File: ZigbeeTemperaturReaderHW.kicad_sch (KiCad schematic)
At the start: 0 parts

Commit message: schema and placed
Draw full schematic (ESP32-C6-Zero, OLED, DS18B20 jack connectors,
LDO regulator, battery holder, pairing button, I2C pull-ups) and wire
all nets with global labels and power symbols. Add footprint library
table entries and component reference documentation.

Co-Authored-By: Claude Sonnet 5 <noreply@anthropic.com>
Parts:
- added BAT2: (no value), Mechanical:BatteryHolder_3xAAA, symbol Mechanical:BatteryHolder_3xAAA
- added C1, C2, C4, C5: CC1206KRX7R9BB104, symbol Passive:Capacitor
- added C6: CC1206KKX7RDBB102, symbol Passive:Capacitor
- added JP1, JP2: (no value), Connectors:JY039-5P, symbol Connector:JY039-5P
- added OLED2: (no value), Modules:OLED-0.96-SSD1306-I2C, symbol Modules:OLED096
- added R1, R2, R3, R4: RC1206JR-7W1RLC19632287, symbol Passive:Resistor
- added S2: TL1105BF160Q, Mechanical:SW_TL1105BF160Q, symbol Mechanical:TL1105BF160Q
- added U1: (no value), Modules:Waveshare-ESP32-C6-Zero, symbol Modules:Waveshare-ESP32-C6-Zero
- added U2: RT9080-33GJ5, Power:TSOT-23-5_RIT-L, symbol Power:RT9080-33GJ5
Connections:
- new net: BAT2.1 (VCC4V5), C2.1, U2.1 (VIN), U2.3 (EN)
- new net GND: BAT2.2 (GND), C1.2, C2.2, C4.2, C5.2, C6.2, JP1.1, JP2.1, OLED2.1 (GND), S2.3, S2.4, U1.2 (GND), U2.2 (GND)
- new net OLED_SCL: OLED2.3 (SCL), R3.2, U1.13 (IO19)
- new net OLED_SDA: OLED2.4 (SDA), R2.2, U1.14 (IO18)
- new net ONE_WIRE: C6.1, JP1.3, JP2.3, R1.2, U1.6 (IO2)
- new net PAIRING: C4.1, R4.2, S2.1, S2.2, U1.8 (IO4)
- new net SENSOR_POWER: C5.1, JP1.5, JP2.5, R1.1, U1.7 (IO3)
- new net VCC3V3: C1.1, OLED2.2 (VCC), R2.1, R3.1, R4.1, U1.3 (V3V), U2.5 (VOUT)
- no-connect marks 0 -> 16

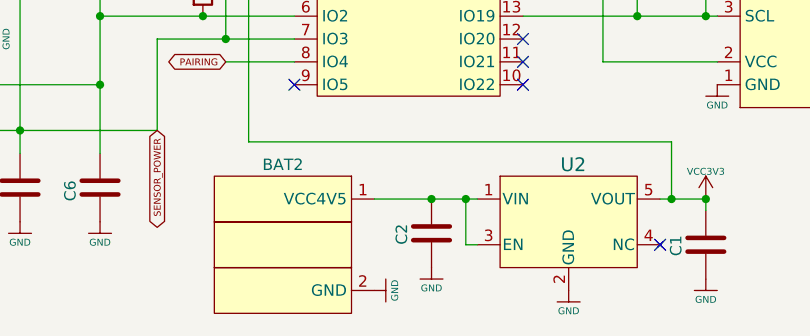
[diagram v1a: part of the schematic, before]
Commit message: Add board dimensions and JLCPCB Gerber/drill export
- Add overall width/height dimension annotations (48.00 x 74.00 mm)
  on the Dwgs.User layer
- Include schematic edits made in the KiCad session
- Add Gerber and Excellon drill files for JLCPCB ordering, plus a
  ready-to-upload ZIP archive

Co-Authored-By: Claude Sonnet 5 <noreply@anthropic.com>
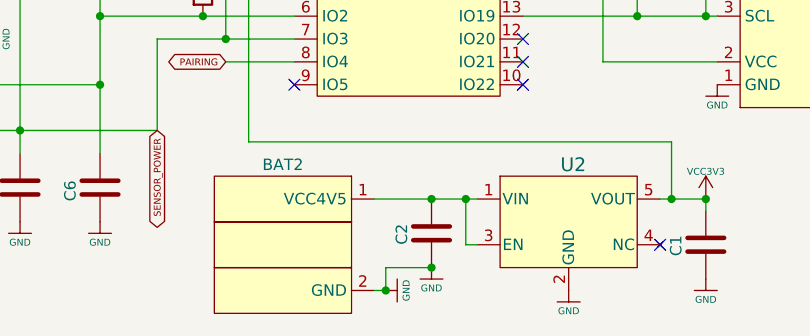
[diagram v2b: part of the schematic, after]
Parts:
- JP1, JP2: value (none) -> FC68133
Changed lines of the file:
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@@
+	)
+	(junction
+		(at 138.43 119.38)
+		(diameter 0)
+		(color 0 0 0 0)
 	)
 	(junction
@@
 	)
 	(junction
+		(at 143.51 116.84)
+		(diameter 0)
+		(color 0 0 0 0)
+	)
+	(junction
 		(at 147.32 109.22)
 		(diameter 0)
@@
 	(wire
 		(pts
+			(xy 138.43 119.38) (xy 137.16 119.38)
+		)
+		(stroke
+			(width 0)
+			(type default)
+		)
+	)
+	(wire
+		(pts
 			(xy 132.08 57.15) (xy 130.81 57.15)
 		)
@@
 	(wire
 		(pts
+			(xy 138.43 116.84) (xy 138.43 119.38)
+		)
+		(stroke
+			(width 0)
+			(type default)
+		)
+	)
+	(wire
+		(pts
 			(xy 148.59 114.3) (xy 147.32 114.3)
 		)
@@
 		(pts
 			(xy 128.27 93.98) (xy 120.65 93.98)
+		)
+		(stroke
+			(width 0)
+			(type default)
+		)
+	)
+	(wire
+		(pts
+			(xy 143.51 116.84) (xy 138.43 116.84)
 		)
 		(stroke
@@
 			)
 		)
-		(property "Value" ""
+		(property "Value" "FC68133"
 			(at 91.44 96.52 0)
+			(hide yes)
 			(show_name no)
 			(do_not_autoplace no)
@@
 			)
 		)
-		(property "Value" ""
+		(property "Value" "FC68133"
 			(at 91.44 81.28 0)
+			(hide yes)
 			(show_name no)
 			(do_not_autoplace no)
@@
 	(symbol
 		(lib_id "Power:GND")
-		(at 137.16 119.38 90)
+		(at 138.43 119.38 90)
 		(unit 1)
 		(body_style 1)
@@
 		(dnp no)
 		(property "Reference" "#PWR015"
-			(at 137.16 119.38 0)
+			(at 138.43 119.38 0)
 			(hide yes)
 			(show_name no)
@@
 		)
 		(property "Value" "GND"
-			(at 139.446 119.38 0)
+			(at 140.716 119.38 0)
 			(show_name no)
 			(do_not_autoplace no)
@@
 		)
 		(property "Footprint" ""
-			(at 137.16 119.38 0)
+			(at 138.43 119.38 0)
 			(hide yes)
 			(show_name no)
@@
 		)
 		(property "Datasheet" ""
-			(at 137.16 119.38 0)
+			(at 138.43 119.38 0)
 			(hide yes)
 			(show_name no)
@@
 		)
 		(property "Description" "Power symbol creates a global label with name \"GNDD\" , digital ground"
-			(at 137.16 119.38 0)
-			(hide yes)
-			(show_name no)
+			(at 138.43 119.38 0)
+			(hide yes)
+			(show_name no)
